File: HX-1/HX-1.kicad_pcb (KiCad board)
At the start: 2 copper layers, 45 x 90 mm, 90 parts, among them J1 USB_C_Receptacle_USB2.0_16P, J10 Conn_01x24, J12 USART, J2 Conn_01x02_Socket, J3 I2C, J4 SPI, J8 UART, J9 Conn_01x24, SW1 BOOT0, U1 STM32H723ZGT6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

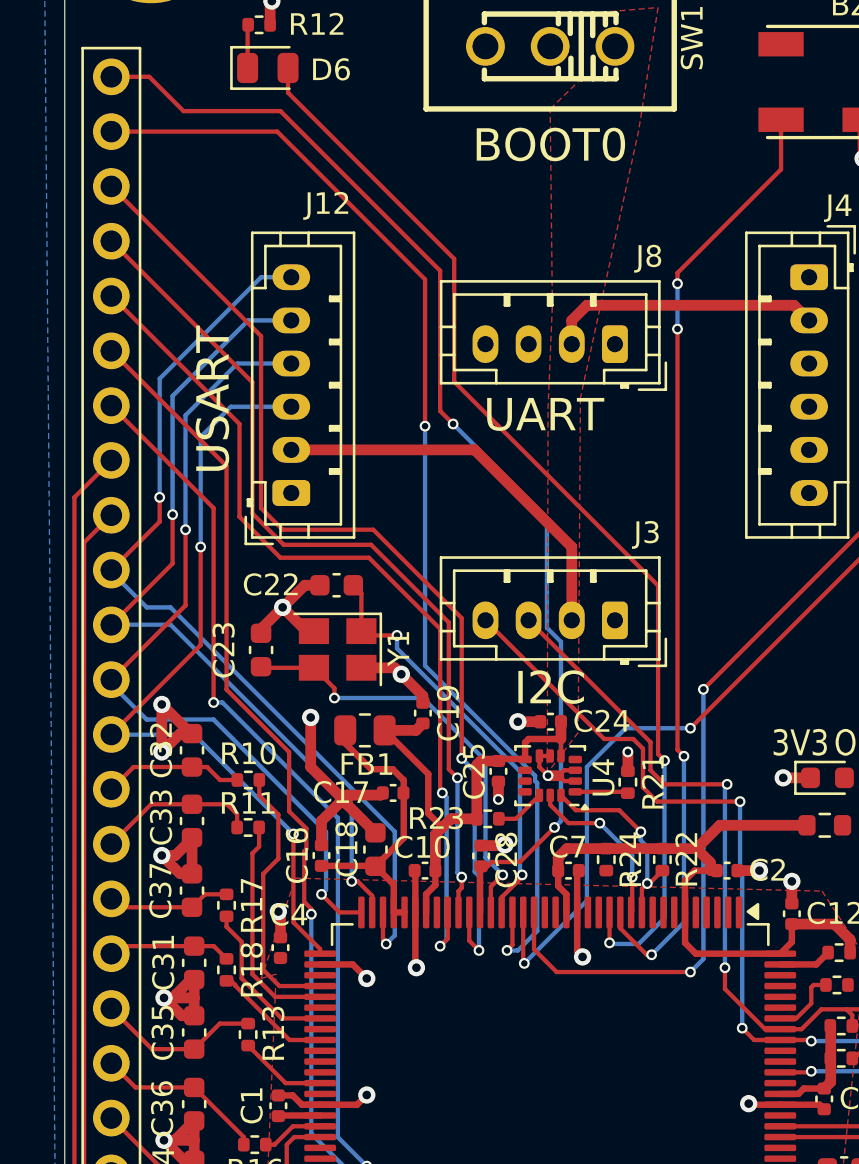
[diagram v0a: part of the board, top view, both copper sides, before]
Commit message: adjust left side traces and components for better ground plane
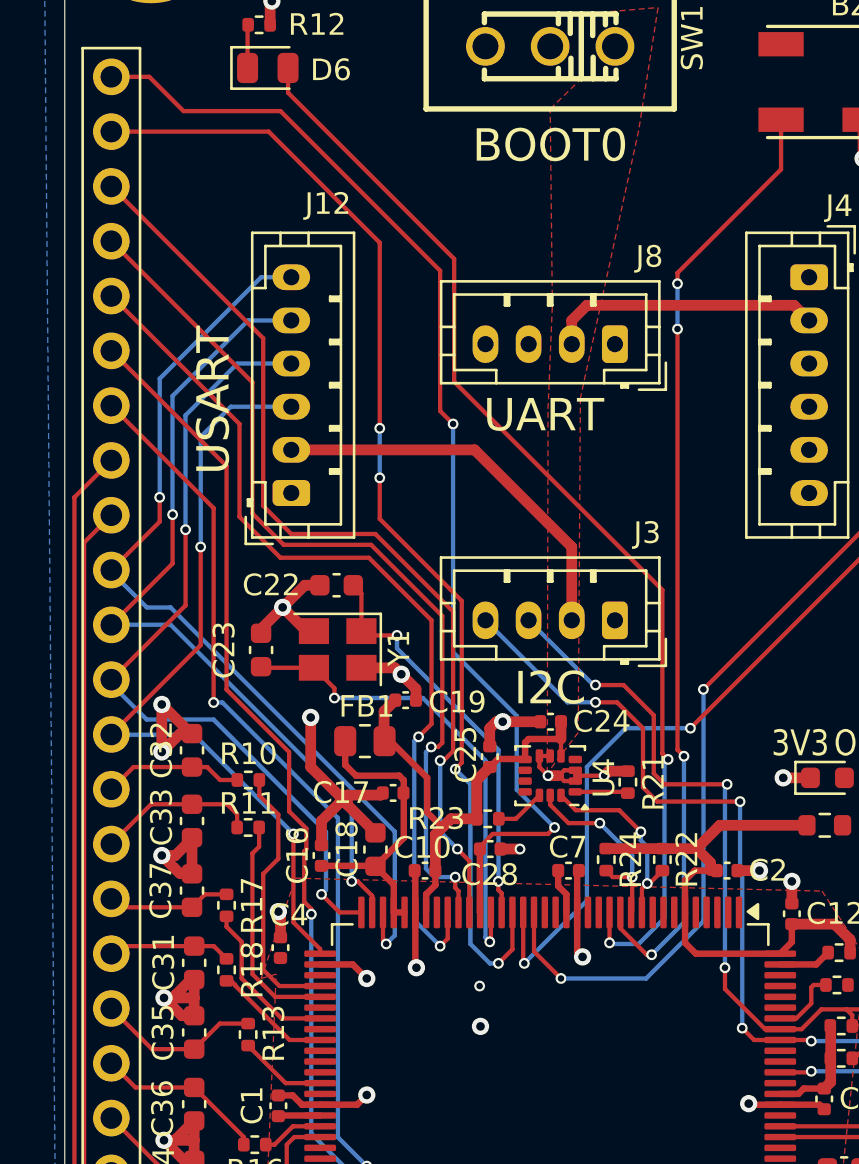
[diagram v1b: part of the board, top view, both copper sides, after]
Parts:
- moved C19 1.00 mm to (142.8, 114.3), turned to 0 degrees
- moved C25 0.79 mm to (146.7, 116.9), turned to 90 degrees
- moved C28 0.53 mm to (146.7, 121.2), turned to 0 degrees
- moved FB1 0.50 mm to (140.9, 116.2)
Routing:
- net +3.3V: track 125.9 -> 122.0 mm
- net GND: track 133.6 -> 137.2 mm, vias 40 -> 41
- net /MCU/GPIO_9: track 46.9 -> 43.4 mm
- net RCC_OSC_OUT: track 20.1 -> 22.3 mm
- net I2C2_SCL: track 7.87 -> 9.19 mm
- net /MCU/GPIO_10: track 40.3 -> 41.5 mm
- net /MCU/I2C_SDA: track 42.9 -> 43.7 mm, vias 2 -> 3
- net RCC_OSC_IN: track 19.6 -> 18.9 mm
- net /MCU/GPIO_6: track 51.5 -> 50.8 mm
- net /MCU/I2C_SCL: track 43.7 -> 44.3 mm, vias 4 -> 5
- net /MCU/GPIO_8: vias 2 -> 4

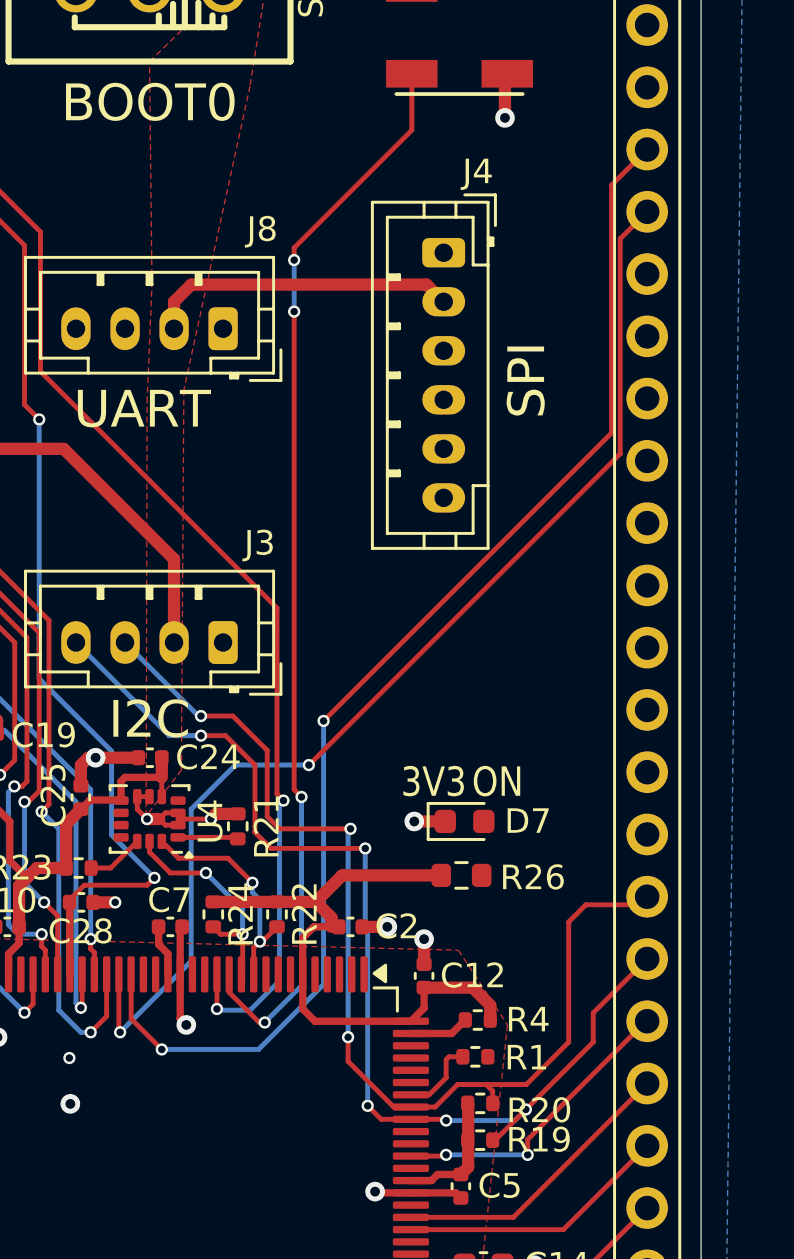
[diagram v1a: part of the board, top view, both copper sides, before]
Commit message: change pin ordering of SPI on left header for better routing, route some of the left traces
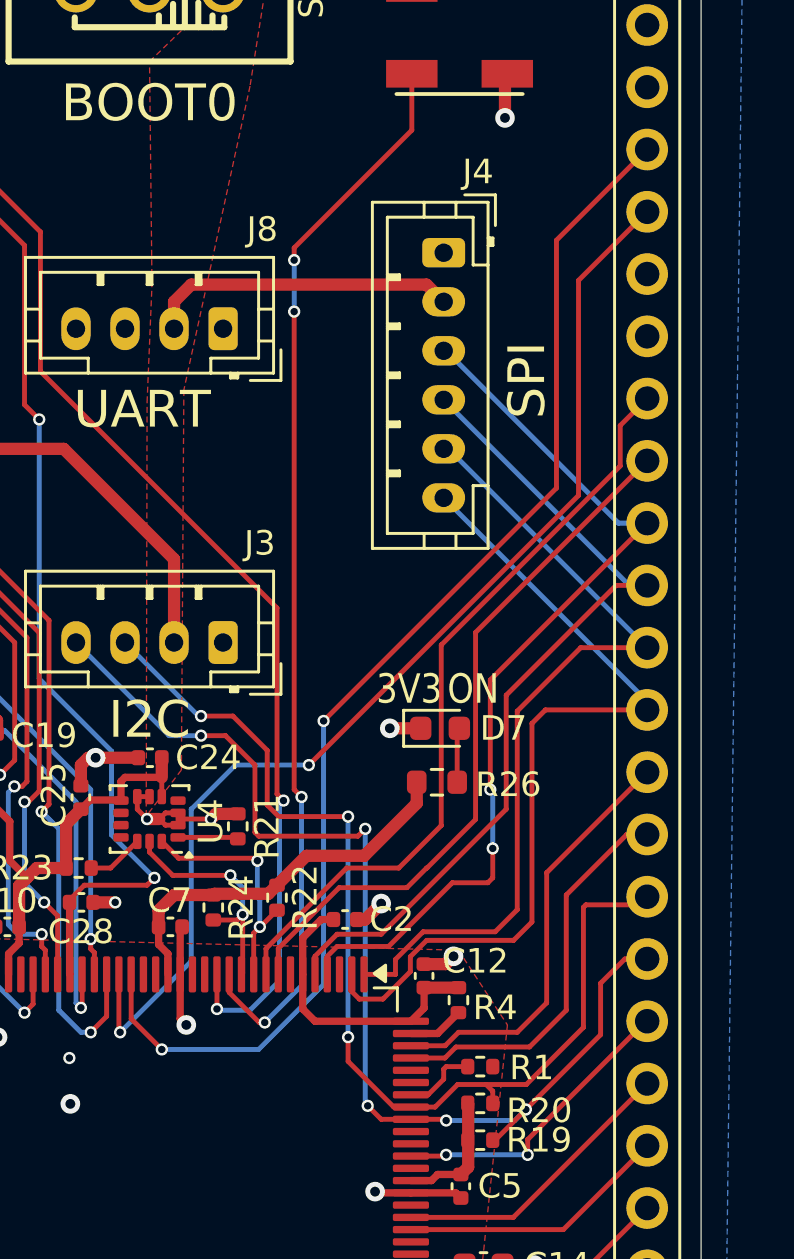
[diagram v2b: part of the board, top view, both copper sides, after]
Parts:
- moved D7 3.93 mm to (161.3, 114.1)
- moved R26 3.93 mm to (161.2, 116.3)
- moved R4 1.13 mm to (162.1, 125.2), turned to -90 degrees
- moved R22 0.68 mm to (154.7, 121.0)
- moved R1 0.45 mm to (163.0, 127.9)
- moved C2 0.37 mm to (157.5, 121.9)
- moved R24 0.28 mm to (152.1, 121.4)
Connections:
- J9 pad 17: /MCU/SPI4_MISO -> /MCU/SPI4_CS
- J9 pad 18: /MCU/SPI4_MOSI -> /MCU/SPI4_SCK
- J9 pad 19: /MCU/SPI4_SCK -> /MCU/SPI4_MOSI
- J9 pad 20: /MCU/SPI4_CS -> /MCU/SPI4_MISO
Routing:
- net /MCU/SPI4_MISO: track 0.00 -> 37.2 mm, vias 0 -> 2
- net /MCU/SPI4_CS: track 0.00 -> 35.0 mm
- net /MCU/SPI4_MOSI: track 0.00 -> 34.7 mm
- net /MCU/SPI4_SCK: track 0.00 -> 33.8 mm
- net /MCU/GPIO_2: track 0.00 -> 31.2 mm
- net /MCU/GPIO_1: track 0.00 -> 28.8 mm
- net /MCU/UART8_TX: track 0.00 -> 17.4 mm
- net /MCU/UART8_RX: track 0.00 -> 16.2 mm
- net /Power Clock IO/3V3_LED: track 0.00 -> 2.24 mm
- net /MCU/I2C_SCL: track 44.3 -> 45.5 mm
- net +3.3V: track 122.0 -> 122.8 mm
- net I2C2_SDA: track 9.31 -> 9.99 mm
- net GND: track 137.2 -> 137.7 mm

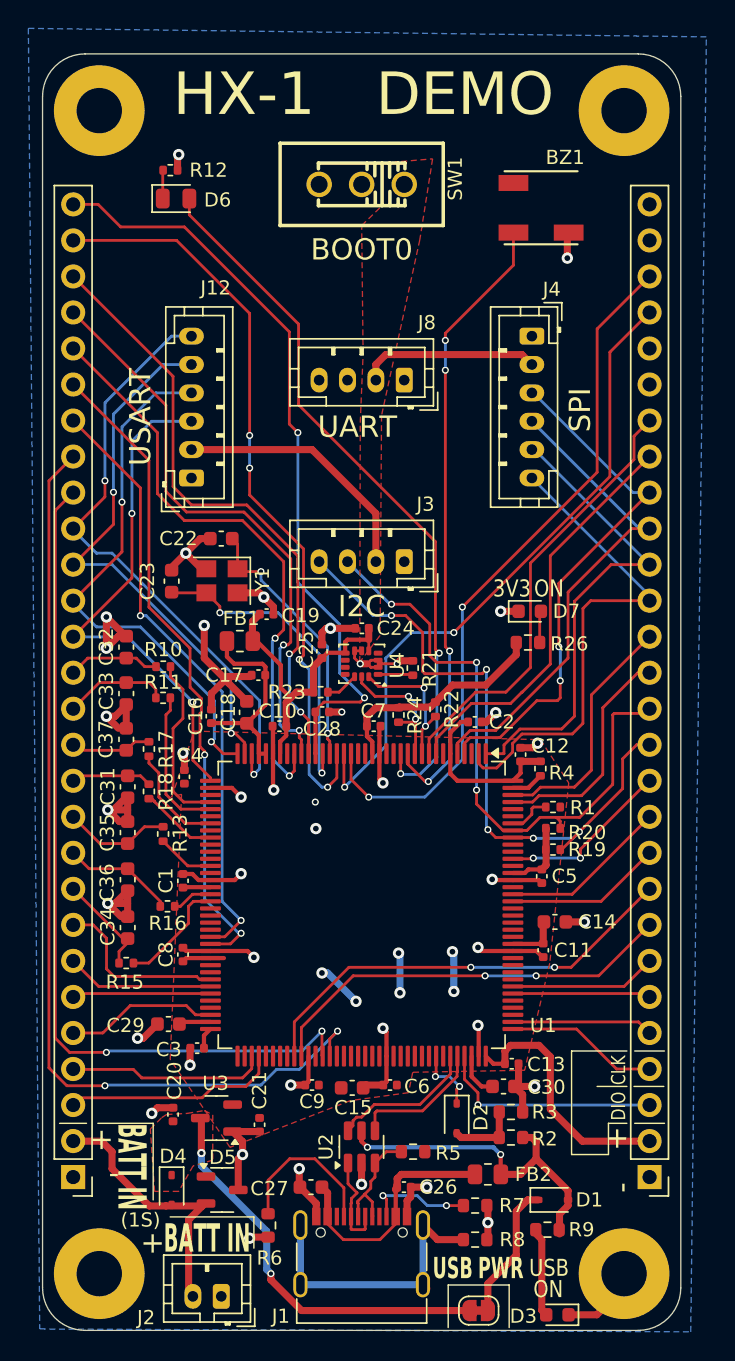
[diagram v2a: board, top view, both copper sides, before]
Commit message: connect remaining traces
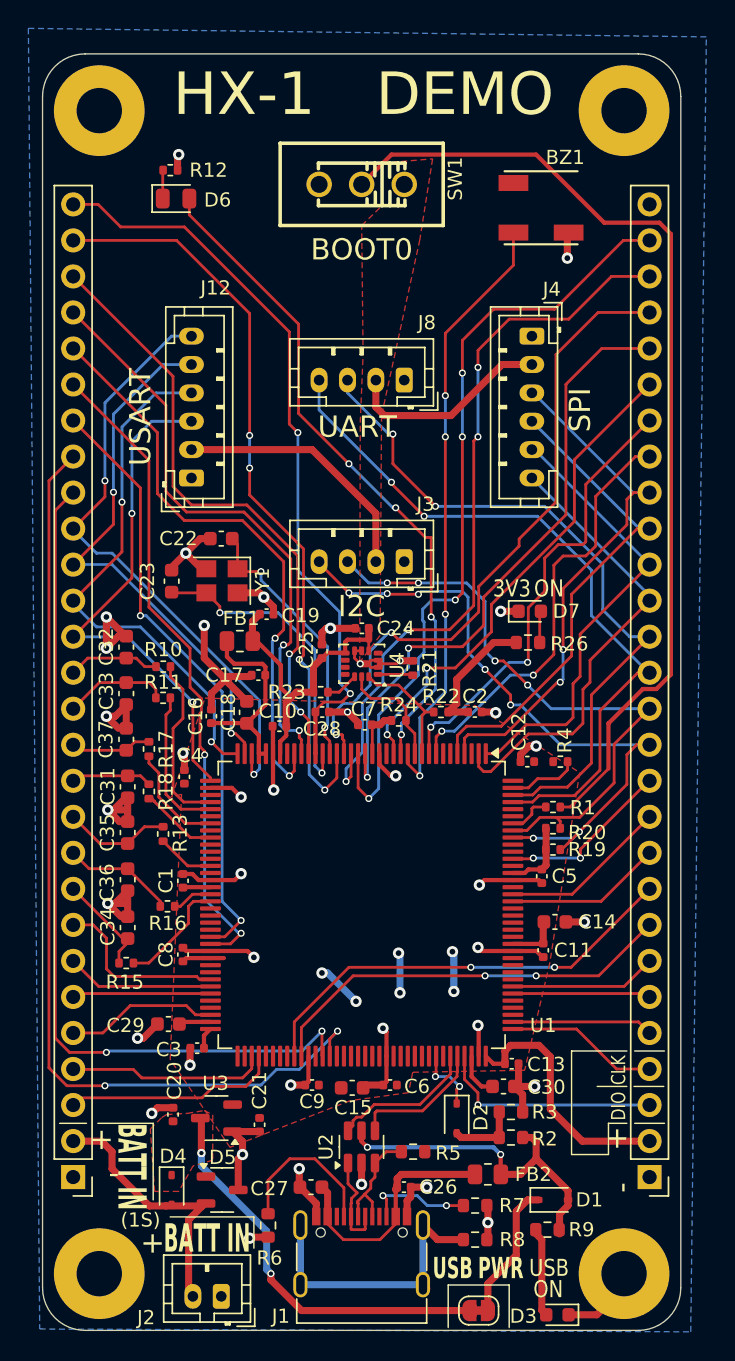
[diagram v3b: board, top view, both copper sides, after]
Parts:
- moved R4 1.49 mm to (163.5, 124.7), turned to 0 degrees
- moved C2 0.70 mm to (157.5, 121.2)
- moved C12 0.69 mm to (161.2, 124.7), turned to 180 degrees
- moved C7 0.64 mm to (149.7, 122.1), turned to 180 degrees
- moved R22 0.43 mm to (155.1, 121.2), turned to 0 degrees
- moved R24 0.39 mm to (152.1, 121.8), turned to 180 degrees
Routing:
- net /MCU/SW_boot0: track 0.00 -> 69.6 mm
- net /MCU/GPIO_5: track 0.00 -> 55.7 mm, vias 0 -> 4
- net /MCU/GPIO_4: track 0.00 -> 44.3 mm, vias 0 -> 2
- net /MCU/GPIO_3: track 0.00 -> 35.0 mm, vias 0 -> 2
- net /MCU/UART8_RX: track 16.2 -> 50.9 mm, vias 0 -> 2
- net /MCU/UART8_TX: track 17.4 -> 49.5 mm, vias 0 -> 2
- net +3.3V: track 122.8 -> 110.0 mm
- net TIM23_LED: track 51.0 -> 47.5 mm, vias 2 -> 4
- net /MCU/PDR_enable: track 2.29 -> 4.96 mm
- net /MCU/SPI4_CS: track 35.0 -> 32.5 mm
- net /MCU/SPI4_SCK: track 33.8 -> 31.9 mm
- net /MCU/NRST: track 53.9 -> 52.3 mm
- net I2C2_SCL: track 9.69 -> 8.10 mm, vias 2 -> 0
- net /MCU/GPIO_2: track 31.2 -> 32.7 mm, vias 0 -> 2
- net /MCU/GPIO_6: track 50.8 -> 52.3 mm, vias 2 -> 4
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
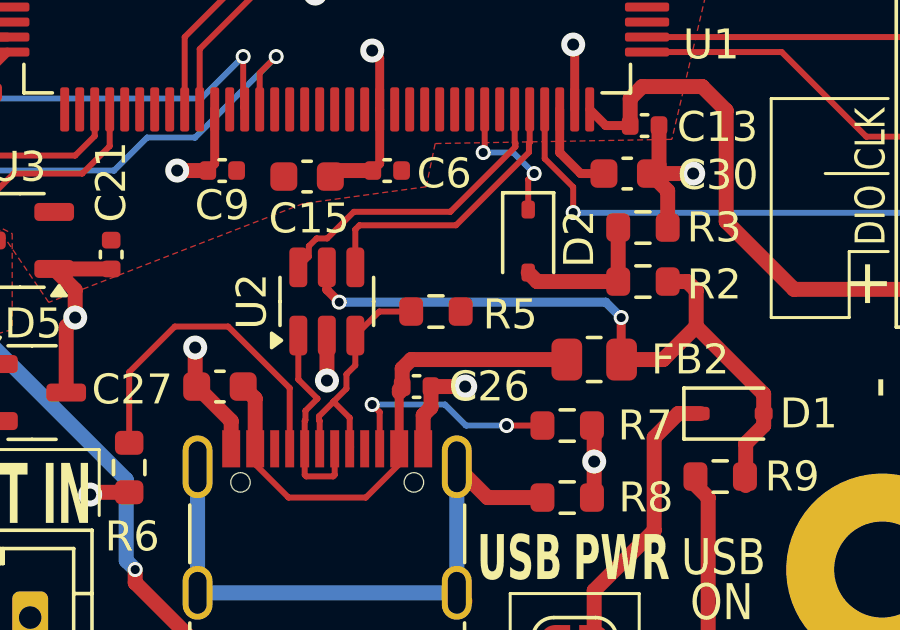
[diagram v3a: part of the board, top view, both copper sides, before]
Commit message: remove unuused pull up resistor on D+ USB, too difficult to trace and unneccesary
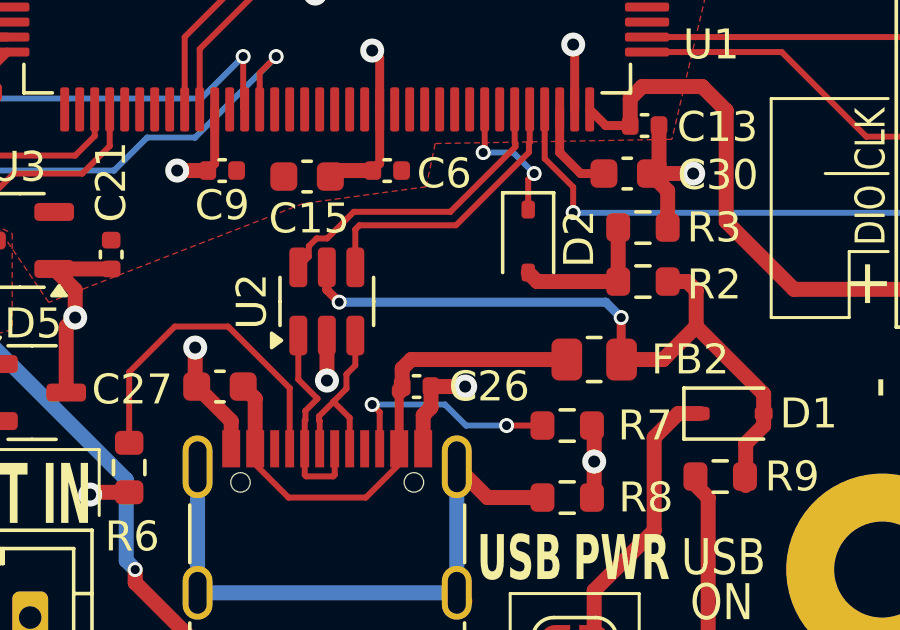
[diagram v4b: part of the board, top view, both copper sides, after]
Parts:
- removed R5: 1k5, Resistor_SMD:R_0603_1608Metric
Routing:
- net /Communication and Debug/D_raw+: track 9.21 -> 7.02 mm
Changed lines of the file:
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@@
 		)
 	)
-	(footprint "Resistor_SMD:R_0603_1608Metric"
-		(layer "F.Cu")
-		(at 153.125 152.2)
-		(descr "Resistor SMD 0603 (1608 Metric), square (rectangular) end terminal, IPC_7351 nominal, (Body size source: IPC-SM-782 page 72, https://www.pcb-3d.com/wordpress/wp-content/uploads/ipc-sm-782a_amendment_1_and_2.pdf), generated with kicad-footprint-generator")
-		(tags "resistor")
-		(property "Reference" "R5"
-			(at 2.475 0.1 0)
-			(layer "F.SilkS")
-			(effects
-				(font
-					(size 1 1)
-					(thickness 0.15)
-				)
-			)
-		)
-		(property "Value" "1k5"
-			(at 0 1.43 0)
-			(layer "F.Fab")
-			(effects
-				(font
-					(size 1 1)
-					(thickness 0.15)
-				)
-			)
-		)
-		(property "Footprint" "Resistor_SMD:R_0603_1608Metric"
-			(at 0 0 0)
-			(unlocked yes)
-			(layer "F.Fab")
-			(hide yes)
-			(effects
-				(font
-					(size 1.27 1.27)
-					(thickness 0.15)
-				)
-			)
-		)
-		(property "Datasheet" ""
-			(at 0 0 0)
-			(unlocked yes)
-			(layer "F.Fab")
-			(hide yes)
-			(effects
-				(font
-					(size 1.27 1.27)
-					(thickness 0.15)
-				)
-			)
-		)
-		(property "Description" "Resistor"
-			(at 0 0 0)
-			(unlocked yes)
-			(layer "F.Fab")
-			(hide yes)
-			(effects
-				(font
-					(size 1.27 1.27)
-					(thickness 0.15)
-				)
-			)
-		)
-		(property "LCSC PN" ""
-			(at 0 0 0)
-			(unlocked yes)
-			(layer "F.Fab")
-			(hide yes)
-			(effects
-				(font
-					(size 1 1)
-					(thickness 0.15)
-				)
-			)
-		)
-		(property ki_fp_filters "R_*")
-		(sheetname "Communication and Debug")
-		(sheetfile "communication_debug.kicad_sch")
-		(attr smd exclude_from_bom dnp)
-		(fp_line
-			(start -0.237258 -0.5225)
-			(end 0.237258 -0.5225)
-			(stroke
-				(width 0.12)
-				(type solid)
-			)
-			(layer "F.SilkS")
-		)
-		(fp_line
-			(start -0.237258 0.5225)
-			(end 0.237258 0.5225)
-			(stroke
-				(width 0.12)
-				(type solid)
-			)
-			(layer "F.SilkS")
-		)
-		(fp_line
-			(start -1.48 -0.73)
-			(end 1.48 -0.73)
-			(stroke
-				(width 0.05)
-				(type solid)
-			)
-			(layer "F.CrtYd")
-		)
-		(fp_line
-			(start -1.48 0.73)
-			(end -1.48 -0.73)
-			(stroke
-				(width 0.05)
-				(type solid)
-			)
-			(layer "F.CrtYd")
-		)
-		(fp_line
-			(start 1.48 -0.73)
-			(end 1.48 0.73)
-			(stroke
-				(width 0.05)
-				(type solid)
-			)
-			(layer "F.CrtYd")
-		)
-		(fp_line
-			(start 1.48 0.73)
-			(end -1.48 0.73)
-			(stroke
-				(width 0.05)
-				(type solid)
-			)
-			(layer "F.CrtYd")
-		)
-		(fp_line
-			(start -0.8 -0.4125)
-			(end 0.8 -0.4125)
-			(stroke
-				(width 0.1)
-				(type solid)
-			)
-			(layer "F.Fab")
-		)
-		(fp_line
-			(start -0.8 0.4125)
-			(end -0.8 -0.4125)
-			(stroke
-				(width 0.1)
-				(type solid)
-			)
-			(layer "F.Fab")
-		)
-		(fp_line
-			(start 0.8 -0.4125)
-			(end 0.8 0.4125)
-			(stroke
-				(width 0.1)
-				(type solid)
-			)
-			(layer "F.Fab")
-		)
-		(fp_line
-			(start 0.8 0.4125)
-			(end -0.8 0.4125)
-			(stroke
-				(width 0.1)
-				(type solid)
-			)
-			(layer "F.Fab")
-		)
-		(fp_text user "${REFERENCE}"
-			(at 0 0 0)
-			(layer "F.Fab")
-			(effects
-				(font
-					(size 0.4 0.4)
-					(thickness 0.06)
-				)
-			)
-		)
-		(pad "1" smd roundrect
-			(at -0.825 0)
-			(size 0.8 0.95)
-			(layers "F.Cu" "F.Paste" "F.Mask")
-			(roundrect_rratio 0.25)
-			(net 94 "/Communication and Debug/D_raw+")
-			(pintype "passive")
-		)
-		(pad "2" smd roundrect
-			(at 0.825 0)
-			(size 0.8 0.95)
-			(layers "F.Cu" "F.Paste" "F.Mask")
-			(roundrect_rratio 0.25)
-			(net 1 "+3.3V")
-			(pintype "passive")
-		)
-		(model "${KICAD8_3DMODEL_DIR}/Resistor_SMD.3dshapes/R_0603_1608Metric.wrl"
-			(offset
-				(xyz 0 0 0)
-			)
-			(scale
-				(xyz 1 1 1)
-			)
-			(rotate
-				(xyz 0 0 0)
-			)
-		)
-	)
 	(footprint "Resistor_SMD:R_0402_1005Metric"
 		(layer "F.Cu")
@@
 	)
 	(segment
-		(start 151.2375 152.2)
-		(end 150.4375 153)
-		(width 0.2)
-		(layer "F.Cu")
-		(net 94)
-	)
-	(segment
 		(start 149.225 155.6932)
 		(end 149.225 155.819999)
@@
 		(width 0.2)
 		(layer "F.Cu")
-		(net 94)
-	)
-	(segment
-		(start 152.3 152.2)
-		(end 151.2375 152.2)
-		(width 0.2)
-		(layer "F.Cu")
